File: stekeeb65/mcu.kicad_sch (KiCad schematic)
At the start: 15 parts, among them IC0 ATMEGA32U4-AU, SW0 SW_Push, Y0 16MHz

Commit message: Started layout for keyboard. still need to verify LED driver schematic
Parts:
- C0, C1, C2, C3, C4, C5, C6, C7: footprint Capacitor_SMD:C_0805_2012Metric_Pad1.18x1.45mm_HandSolder -> Capacitor_SMD:C_0603_1608Metric_Pad1.08x0.95mm_HandSolder
- R0, R1, R2: footprint Resistor_SMD:R_0805_2012Metric_Pad1.20x1.40mm_HandSolder -> Resistor_SMD:R_0603_1608Metric_Pad0.98x0.95mm_HandSolder
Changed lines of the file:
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@@
       (effects (font (size 1.27 1.27)) (justify right))
     )
-    (property "Footprint" "Resistor_SMD:R_0805_2012Metric_Pad1.20x1.40mm_HandSolder" (id 2) (at 183.134 81.026 90)
+    (property "Footprint" "Resistor_SMD:R_0603_1608Metric_Pad0.98x0.95mm_HandSolder" (id 2) (at 183.134 81.026 90)
       (effects (font (size 1.27 1.27)) hide)
     )
@@
       (effects (font (size 1.27 1.27)) (justify left))
     )
-    (property "Footprint" "Capacitor_SMD:C_0805_2012Metric_Pad1.18x1.45mm_HandSolder" (id 2) (at 26.3652 176.53 0)
+    (property "Footprint" "Capacitor_SMD:C_0603_1608Metric_Pad1.08x0.95mm_HandSolder" (id 2) (at 26.3652 176.53 0)
       (effects (font (size 1.27 1.27)) hide)
     )
@@
       (effects (font (size 1.27 1.27)) (justify left))
     )
-    (property "Footprint" "Capacitor_SMD:C_0805_2012Metric_Pad1.18x1.45mm_HandSolder" (id 2) (at 72.0852 176.53 0)
+    (property "Footprint" "Capacitor_SMD:C_0603_1608Metric_Pad1.08x0.95mm_HandSolder" (id 2) (at 72.0852 176.53 0)
       (effects (font (size 1.27 1.27)) hide)
     )
@@
       (effects (font (size 1.27 1.27)) (justify left))
     )
-    (property "Footprint" "Capacitor_SMD:C_0805_2012Metric_Pad1.18x1.45mm_HandSolder" (id 2) (at 60.6552 176.53 0)
+    (property "Footprint" "Capacitor_SMD:C_0603_1608Metric_Pad1.08x0.95mm_HandSolder" (id 2) (at 60.6552 176.53 0)
       (effects (font (size 1.27 1.27)) hide)
     )
@@
     (property "Reference" "R1" (id 0) (at 69.85 134.62 90))
     (property "Value" "22" (id 1) (at 69.85 137.16 90))
-    (property "Footprint" "Resistor_SMD:R_0805_2012Metric_Pad1.20x1.40mm_HandSolder" (id 2) (at 70.104 139.954 90)
+    (property "Footprint" "Resistor_SMD:R_0603_1608Metric_Pad0.98x0.95mm_HandSolder" (id 2) (at 70.104 139.954 90)
       (effects (font (size 1.27 1.27)) hide)
     )
@@
     (property "Reference" "R2" (id 0) (at 76.2 146.05 90))
     (property "Value" "22" (id 1) (at 76.2 148.59 90))
-    (property "Footprint" "Resistor_SMD:R_0805_2012Metric_Pad1.20x1.40mm_HandSolder" (id 2) (at 75.946 144.526 90)
+    (property "Footprint" "Resistor_SMD:R_0603_1608Metric_Pad0.98x0.95mm_HandSolder" (id 2) (at 75.946 144.526 90)
       (effects (font (size 1.27 1.27)) hide)
     )
@@
     (property "Reference" "C2" (id 0) (at 143.51 138.43 90))
     (property "Value" "1u" (id 1) (at 143.51 140.97 90))
-    (property "Footprint" "Capacitor_SMD:C_0805_2012Metric_Pad1.18x1.45mm_HandSolder" (id 2) (at 139.7 147.0152 0)
+    (property "Footprint" "Capacitor_SMD:C_0603_1608Metric_Pad1.08x0.95mm_HandSolder" (id 2) (at 139.7 147.0152 0)
       (effects (font (size 1.27 1.27)) hide)
     )
@@
       (effects (font (size 1.27 1.27)) (justify left))
     )
-    (property "Footprint" "Capacitor_SMD:C_0805_2012Metric_Pad1.18x1.45mm_HandSolder" (id 2) (at 91.1352 147.32 0)
+    (property "Footprint" "Capacitor_SMD:C_0603_1608Metric_Pad1.08x0.95mm_HandSolder" (id 2) (at 91.1352 147.32 0)
       (effects (font (size 1.27 1.27)) hide)
     )
@@
       (effects (font (size 1.27 1.27)) (justify left))
     )
-    (property "Footprint" "Capacitor_SMD:C_0805_2012Metric_Pad1.18x1.45mm_HandSolder" (id 2) (at 37.7952 176.53 0)
+    (property "Footprint" "Capacitor_SMD:C_0603_1608Metric_Pad1.08x0.95mm_HandSolder" (id 2) (at 37.7952 176.53 0)
       (effects (font (size 1.27 1.27)) hide)
     )
@@
     (property "Reference" "C0" (id 0) (at 143.51 121.92 90))
     (property "Value" "1u" (id 1) (at 143.51 124.46 90))
-    (property "Footprint" "Capacitor_SMD:C_0805_2012Metric_Pad1.18x1.45mm_HandSolder" (id 2) (at 139.7 130.5052 0)
+    (property "Footprint" "Capacitor_SMD:C_0603_1608Metric_Pad1.08x0.95mm_HandSolder" (id 2) (at 139.7 130.5052 0)
       (effects (font (size 1.27 1.27)) hide)
     )
@@
       (effects (font (size 1.27 1.27)) (justify left))
     )
-    (property "Footprint" "Capacitor_SMD:C_0805_2012Metric_Pad1.18x1.45mm_HandSolder" (id 2) (at 49.2252 176.53 0)
-      (effects (font (size 1.27 1.27)) hide)
-    )
+    (property "Footprint" "Capacitor_SMD:C_0603_1608Metric_Pad1.08x0.95mm_HandSolder" (id 2) (at 49.2252 176.53 0)
+      (effects (font (size 1.27 1.27)) hide)
+    )

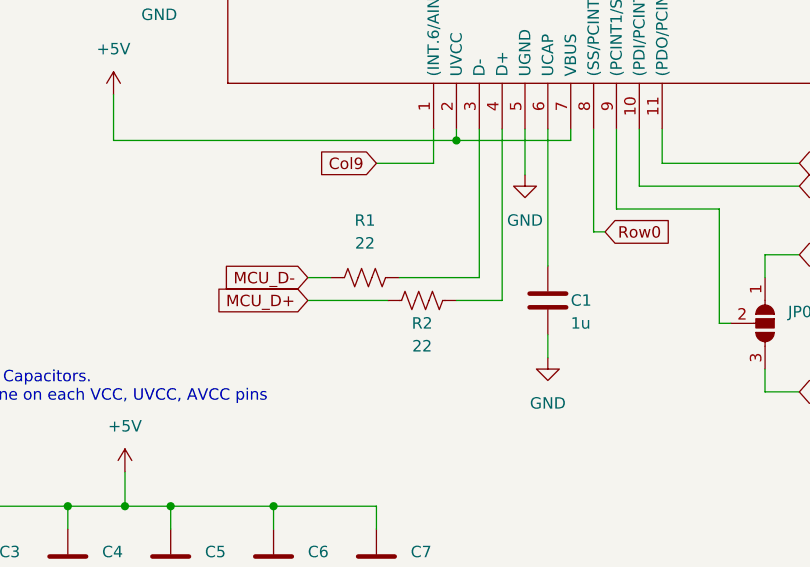
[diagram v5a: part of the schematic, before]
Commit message: Replacing Type-C in lieu of a daughter board connector.
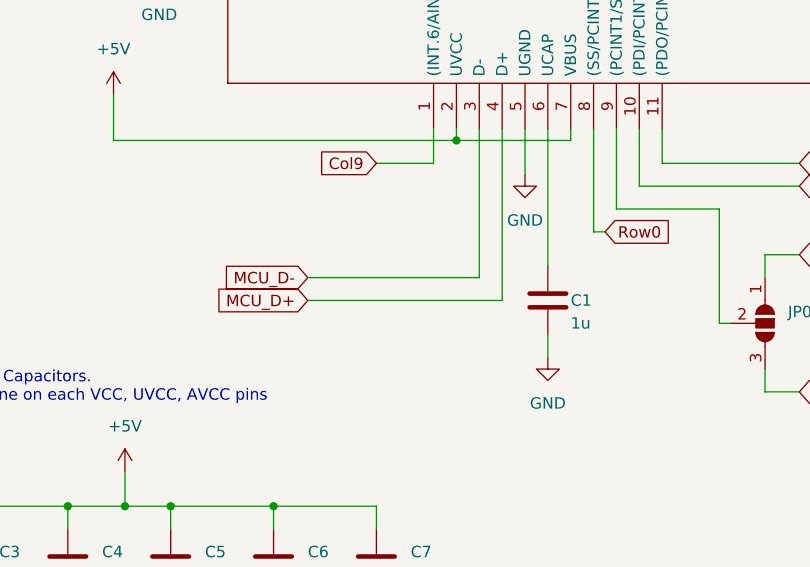
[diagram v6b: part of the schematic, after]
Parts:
- removed R1, R2: 22, Resistor_SMD:R_0603_1608Metric_Pad0.98x0.95mm_HandSolder, symbol Device:R_US
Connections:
- net MCU_D+: now also IC0.4 (D+)
- net MCU_D-: now also IC0.3 (D-)
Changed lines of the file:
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@@
-    (stroke (width 0) (type default) (color 0 0 0 0))
-  )
-  (wire (pts (xy 63.5 140.97) (xy 66.04 140.97))
     (stroke (width 0) (type default) (color 0 0 0 0))
   )
@@
     (stroke (width 0) (type default) (color 0 0 0 0))
   )
-  (wire (pts (xy 80.01 143.51) (xy 85.09 143.51))
-    (stroke (width 0) (type default) (color 0 0 0 0))
-  )
   (wire (pts (xy 109.22 146.05) (xy 110.49 146.05))
     (stroke (width 0) (type default) (color 0 0 0 0))
@@
     (stroke (width 0) (type default) (color 0 0 0 0))
   )
-  (wire (pts (xy 63.5 143.51) (xy 72.39 143.51))
+  (wire (pts (xy 63.5 143.51) (xy 85.09 143.51))
     (stroke (width 0) (type default) (color 0 0 0 0))
   )
@@
     (stroke (width 0) (type default) (color 0 0 0 0))
   )
-  (wire (pts (xy 73.66 140.97) (xy 82.55 140.97))
+  (wire (pts (xy 63.5 140.97) (xy 82.55 140.97))
     (stroke (width 0) (type default) (color 0 0 0 0))
   )
@@
     )
     (pin "1")
-  )
-  (symbol (lib_id "Device:R_US") (at 69.85 140.97 90) (unit 1)
-    (in_bom yes) (on_board yes) (fields_autoplaced)
-    (property "Reference" "R1" (id 0) (at 69.85 134.62 90))
-    (property "Value" "22" (id 1) (at 69.85 137.16 90))
-    (property "Footprint" "Resistor_SMD:R_0603_1608Metric_Pad0.98x0.95mm_HandSolder" (id 2) (at 70.104 139.954 90)
-      (effects (font (size 1.27 1.27)) hide)
-    )
-    (property "Datasheet" "~" (id 3) (at 69.85 140.97 0)
-      (effects (font (size 1.27 1.27)) hide)
-    )
-    (pin "1")
-    (pin "2")
   )
   (symbol (lib_id "power:GND") (at 107.95 41.91 90) (unit 1)
@@
     (pin "1")
   )
-  (symbol (lib_id "Device:R_US") (at 76.2 143.51 270) (unit 1)
-    (in_bom yes) (on_board yes)
-    (property "Reference" "R2" (id 0) (at 76.2 146.05 90))
-    (property "Value" "22" (id 1) (at 76.2 148.59 90))
-    (property "Footprint" "Resistor_SMD:R_0603_1608Metric_Pad0.98x0.95mm_HandSolder" (id 2) (at 75.946 144.526 90)
-      (effects (font (size 1.27 1.27)) hide)
-    )
-    (property "Datasheet" "~" (id 3) (at 76.2 143.51 0)
-      (effects (font (size 1.27 1.27)) hide)
-    )
-    (pin "1")
-    (pin "2")
-  )
   (symbol (lib_id "Device:C") (at 143.51 146.05 270) (unit 1)
